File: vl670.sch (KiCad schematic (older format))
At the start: 56 parts, among them J1 Conn_01x07_Male, J2 USB_C_Receptacle, J3 Conn_01x07_Male, J4 USB3_A Receptacle, J5 Conn_01x02_Male, U2 VL670, U4 TPS2061C-PXLI, Y1 25MHz

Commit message: First private release.
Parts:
- removed C15: 1uF, Capacitor_SMD:C_0603_1608Metric_Pad1.08x0.95mm_HandSolder, symbol Device:C
- removed C23, C24: 330nF, Capacitor_SMD:C_0603_1608Metric, symbol Device:C_Small
- removed JP3: SolderJumper_2_Bridged, Jumper:SolderJumper-2_P1.3mm_Bridged_RoundedPad1.0x1.5mm, symbol Jumper:SolderJumper_2_Bridged
- added C7, C8: 220nF, Capacitor_SMD:C_0603_1608Metric_Pad1.08x0.95mm_HandSolder, symbol Device:C_Small
- added R15: 10k, Resistor_SMD:R_0603_1608Metric_Pad0.98x0.95mm_HandSolder, symbol Device:R_US
- added R19: 0R, Resistor_SMD:R_0603_1608Metric_Pad0.98x0.95mm_HandSolder, symbol Device:R_US
- C10, C11: Grade (none) -> NP0
- C31: renamed from C1; value 1uF -> 470nF
- C32: renamed from C2; value 1uF -> 470nF
- C33: renamed from C3; value 1uF -> 470nF
- C34: renamed from C4; value 1uF -> 470nF
- C35: renamed from C5; value 1uF -> 470nF
- D10, D11, D12, D13, D15, D16, D17, D18, D8, D9: value D_TVS -> ESD7951S; footprint Diode_SMD:D_SOD-923 -> Diode_SMD:D_SOD-523
- D14, D7: footprint Diode_SMD:D_SOD-923 -> Diode_SMD:D_SOD-523
- J2: footprint Connector_USB:USB_C_Receptacle_Amphenol_12401548E4-2A -> vl670:USB_C_Receptacle_XKB_U262-241N-4BV60
- J4: footprint Connector_USB:USB3_A_Molex_48393-001 -> vl670:USB3_A_Receptacle_Wuerth_692112030100_Horizontal
- L1: footprint Inductor_SMD:L_0603_1608Metric_Pad1.05x0.95mm_HandSolder -> Inductor_SMD:L_1008_2520Metric_Pad1.43x2.20mm_HandSolder; Brand (none) -> L1: Sunlord; Part Number (none) -> SPH252012H4R7MT
- renumbered C6 to C41, C7 to C42, C8 to C43, C9 to C44, C17 to C51, C18 to C52, C14 to C61, C16 to C62
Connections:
- net labels added: DN_SSRX+, DN_SSRX-, DN_SSTX+, DN_SSTX-, DN_TX_AC+, DN_TX_AC-, D_DEMUX+, D_DEMUX-, SSRX_DEMUX+, SSRX_DEMUX-, SSTX_DEMUX+, SSTX_DEMUX-, ~EXT_RESET
- net labels removed: D+, D-, DN_USB3RX+, DN_USB3RX-, DN_USB3TX+, DN_USB3TX-, TX+, TX-
- wire segments 313 -> 319
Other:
- note added: "By default, both VL670 and ISP header\nare connected, to allow probing SPI\nwhile VL670 is running.\n\nTo program the EEPROM, a programmer\nmust pull ~ISP_ENABLE~ low from the ISP\nheader (bridge pin 6 & 7 on J1), to\navoid bus contention."
- note added: "C44 MUST be close to L1"
- note added: "PCB\nlayout-specific\n components"
- note added: "close to VL670, one per pin"
- note removed: "By default, both VL670 and ISP header\nare connected, to allow probing SPI\nwhile VL670 is running.\n\nTo program the EEPROM, a programmer\nmust pull ~ISP_ENABLE~ low from the ISP\nheader, to avoid bus contention."
- moved on the sheet: C13, C31, C32, C33, C34, C35, C41, C42, C43, C44, C51, C52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

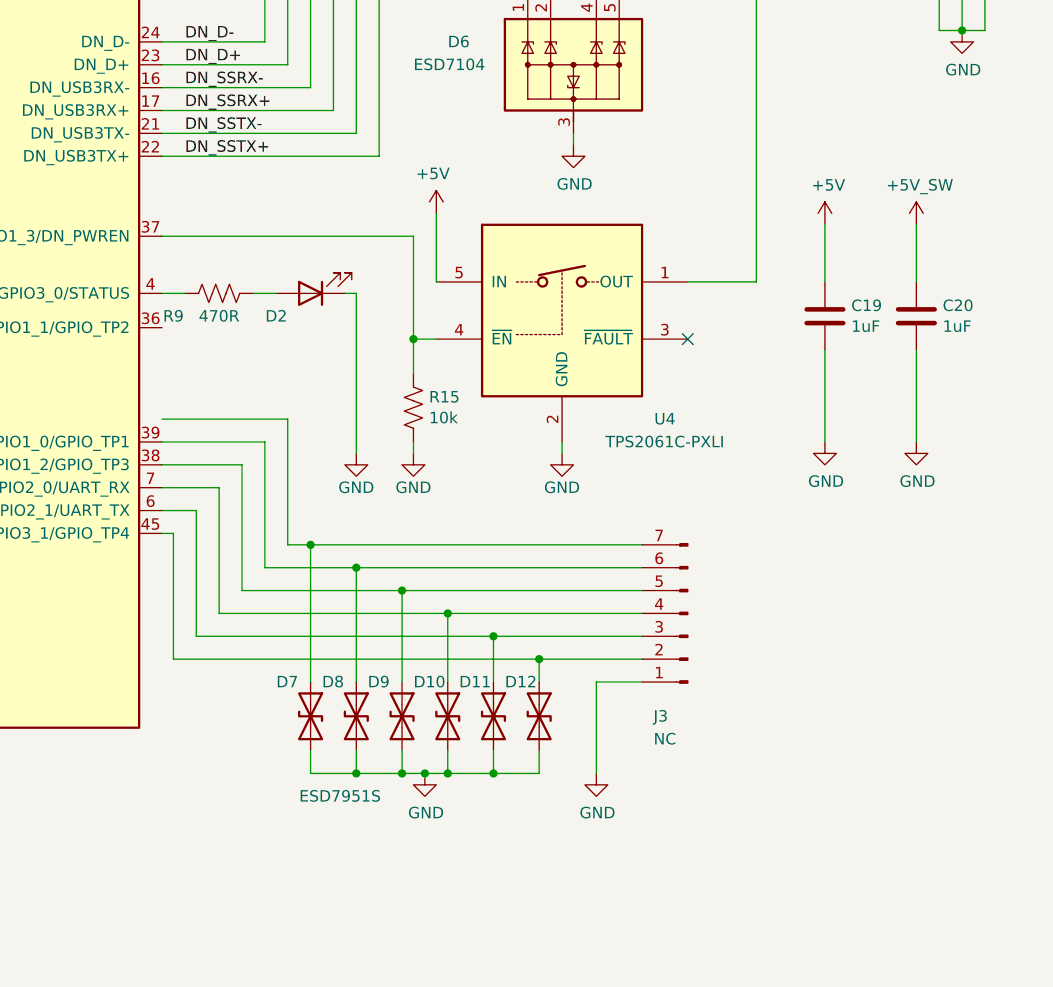
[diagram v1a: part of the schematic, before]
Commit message: Change GPIO connections to match firmware.
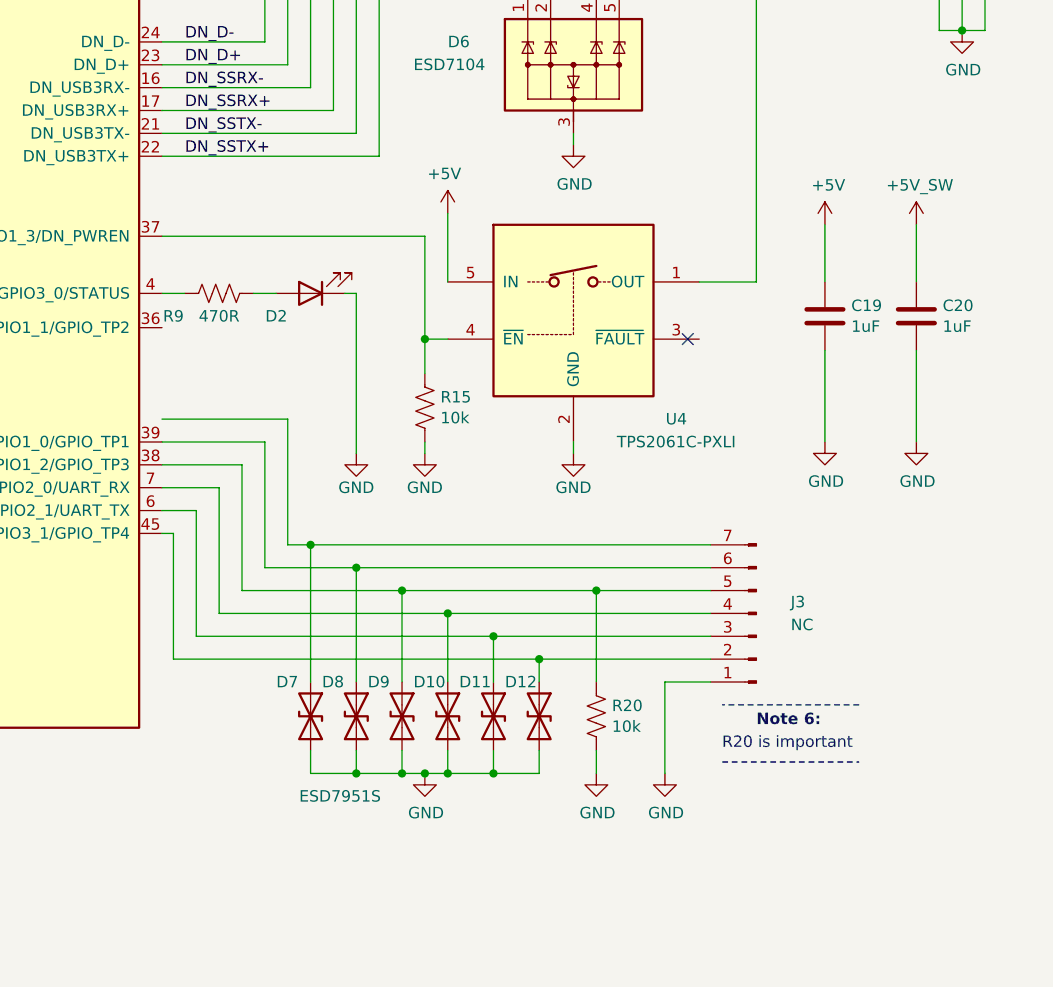
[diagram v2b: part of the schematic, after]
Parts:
- added R20: 10k, Resistor_SMD:R_0603_1608Metric_Pad0.98x0.95mm_HandSolder, symbol Device:R_US
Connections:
- net GND: now also R20.2
- net at D9.1 (A1), J3.5 (Pin_5), U2.38 (GPIO1_2/GPIO_TP3): now also R20.1
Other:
- note added: "Note 6:"
- note added: "R20 is important"
- moved on the sheet: J3, R15, U4
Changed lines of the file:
@@
 L power:GND #PWR0115
 U 1 1 60701D89
-P 9050 4900
-F 0 "#PWR0115" H 9050 4650 50  0001 C CNN
-F 1 "GND" H 9050 4750 50  0000 C CNN
-F 2 "" H 9050 4900 50  0001 C CNN
-F 3 "" H 9050 4900 50  0001 C CNN
-	1    9050 4900
+P 9100 4900
+F 0 "#PWR0115" H 9100 4650 50  0001 C CNN
+F 1 "GND" H 9100 4750 50  0000 C CNN
+F 2 "" H 9100 4900 50  0001 C CNN
+F 3 "" H 9100 4900 50  0001 C CNN
+	1    9100 4900
 	-1   0    0    -1
 $EndComp
@@
 L Connector:Conn_01x07_Male J3
 U 1 1 61CF71E3
-P 9600 5600
-F 0 "J3" H 9750 6050 50  0000 R CNN
-F 1 "Conn_01x07_Male" H 9572 5623 50  0001 R CNN
-F 2 "Connector_PinHeader_2.54mm:PinHeader_1x07_P2.54mm_Vertical" H 9600 5600 50  0001 C CNN
-F 3 "~" H 9600 5600 50  0001 C CNN
-F 4 "NC" H 9700 6150 50  0000 C CNN "Install"
-	1    9600 5600
+P 9900 5600
+F 0 "J3" H 9750 5550 50  0000 R CNN
+F 1 "Conn_01x07_Male" H 9872 5623 50  0001 R CNN
+F 2 "Connector_PinHeader_2.54mm:PinHeader_1x07_P2.54mm_Vertical" H 9900 5600 50  0001 C CNN
+F 3 "~" H 9900 5600 50  0001 C CNN
+F 4 "NC" H 9700 5650 50  0000 C CNN "Install"
+	1    9900 5600
 	-1   0    0    1
 $EndComp
@@
 L vl670:TPS2061C U4
 U 1 1 605C86BA
-P 9050 4200
-F 0 "U4" H 9500 3650 50  0000 C CNN
-F 1 "TPS2061C-PXLI" H 9500 3550 50  0000 C CNN
-F 2 "Package_TO_SOT_SMD:SOT-23-5_HandSoldering" H 9050 4700 50  0001 C CNN
-F 3 "https://www.ti.com/lit/gpn/tps2061c" H 9000 4500 50  0001 C CNN
-	1    9050 4200
+P 9100 4200
+F 0 "U4" H 9550 3650 50  0000 C CNN
+F 1 "TPS2061C-PXLI" H 9550 3550 50  0000 C CNN
+F 2 "Package_TO_SOT_SMD:SOT-23-5_HandSoldering" H 9100 4700 50  0001 C CNN
+F 3 "https://www.ti.com/lit/gpn/tps2061c" H 9050 4500 50  0001 C CNN
+	1    9100 4200
 	1    0    0    -1
 $EndComp
@@
 L power:GND #PWR0126
 U 1 1 60071875
-P 9200 6300
-F 0 "#PWR0126" H 9200 6050 50  0001 C CNN
-F 1 "GND" H 9205 6127 50  0000 C CNN
-F 2 "" H 9200 6300 50  0001 C CNN
-F 3 "" H 9200 6300 50  0001 C CNN
-	1    9200 6300
-	1    0    0    -1
-$EndComp
-Wire Wire Line
-	9200 5900 9400 5900
-Wire Wire Line
-	8400 3950 8400 4400
-Wire Wire Line
-	7300 3950 8400 3950
-Wire Wire Line
-	8400 4400 8500 4400
+P 9500 6300
+F 0 "#PWR0126" H 9500 6050 50  0001 C CNN
+F 1 "GND" H 9505 6127 50  0000 C CNN
+F 2 "" H 9500 6300 50  0001 C CNN
+F 3 "" H 9500 6300 50  0001 C CNN
+	1    9500 6300
+	1    0    0    -1
+$EndComp
+Wire Wire Line
+	9500 5900 9700 5900
 Wire Wire Line
 	7300 4200 7400 4200
@@
 L power:+5V #PWR0112
 U 1 1 605CDF9A
-P 8500 3850
-F 0 "#PWR0112" H 8500 3700 50  0001 C CNN
-F 1 "+5V" H 8515 4023 50  0000 C CNN
-F 2 "" H 8500 3850 50  0001 C CNN
-F 3 "" H 8500 3850 50  0001 C CNN
-	1    8500 3850
+P 8550 3850
+F 0 "#PWR0112" H 8550 3700 50  0001 C CNN
+F 1 "+5V" H 8565 4023 50  0000 C CNN
+F 2 "" H 8550 3850 50  0001 C CNN
+F 3 "" H 8550 3850 50  0001 C CNN
+	1    8550 3850
 	-1   0    0    -1
 $EndComp
@@
 	1    0    0    -1
 $EndComp
-Wire Wire Line
-	9600 4150 9900 4150
 Connection ~ 9900 1800
 Wire Wire Line
@@
 Connection ~ 8950 5800
 Wire Wire Line
-	8950 5800 9400 5800
-Wire Wire Line
-	8750 5700 9400 5700
-Wire Wire Line
-	8550 5600 9400 5600
-Wire Wire Line
-	8350 5500 9400 5500
-Wire Wire Line
-	8150 5400 9400 5400
-Wire Wire Line
-	7950 5300 9400 5300
-Wire Wire Line
-	9200 5900 9200 6300
+	9500 5900 9500 6300
 Wire Wire Line
 	7950 6300 8150 6300
@@
 	6600 1800 6700 1800
 Wire Wire Line
-	8500 3850 8500 4150
-Wire Wire Line
-	9050 4850 9050 4900
+	8550 3850 8550 4150
+Wire Wire Line
+	9100 4850 9100 4900
 Wire Wire Line
 	8150 4200 8150 4900
@@
 	1    0    0    -1
 $EndComp
-Connection ~ 8400 4400
 $Comp
 L Device:R_US R15
 U 1 1 608A3AA8
-P 8400 4700
-F 0 "R15" H 8468 4746 50  0000 L CNN
-F 1 "10k" H 8468 4655 50  0000 L CNN
-F 2 "Resistor_SMD:R_0603_1608Metric_Pad0.98x0.95mm_HandSolder" V 8440 4690 50  0001 C CNN
-F 3 "~" H 8400 4700 50  0001 C CNN
-	1    8400 4700
-	1    0    0    -1
-$EndComp
-Wire Wire Line
-	8400 4550 8400 4400
+P 8450 4700
+F 0 "R15" H 8518 4746 50  0000 L CNN
+F 1 "10k" H 8518 4655 50  0000 L CNN
+F 2 "Resistor_SMD:R_0603_1608Metric_Pad0.98x0.95mm_HandSolder" V 8490 4690 50  0001 C CNN
+F 3 "~" H 8450 4700 50  0001 C CNN
+	1    8450 4700
+	1    0    0    -1
+$EndComp
 $Comp
 L power:GND #PWR0111
 U 1 1 608DDF82
-P 8400 4900
-F 0 "#PWR0111" H 8400 4650 50  0001 C CNN
-F 1 "GND" H 8400 4750 50  0000 C CNN
-F 2 "" H 8400 4900 50  0001 C CNN
-F 3 "" H 8400 4900 50  0001 C CNN
-	1    8400 4900
+P 8450 4900
+F 0 "#PWR0111" H 8450 4650 50  0001 C CNN
+F 1 "GND" H 8450 4750 50  0000 C CNN
+F 2 "" H 8450 4900 50  0001 C CNN
+F 3 "" H 8450 4900 50  0001 C CNN
+	1    8450 4900
 	-1   0    0    -1
 $EndComp
 Wire Wire Line
-	8400 4850 8400 4900
+	8450 4850 8450 4900
 Wire Wire Line
 	8150 4200 8100 4200
@@
 Wire Wire Line
 	8900 2550 8800 2750
+$Comp
+L Device:R_US R20
+U 1 1 61D6C1E1
+P 9200 6050
+F 0 "R20" H 9268 6096 50  0000 L CNN
+F 1 "10k" H 9268 6005 50  0000 L CNN
+F 2 "Resistor_SMD:R_0603_1608Metric_Pad0.98x0.95mm_HandSolder" V 9240 6040 50  0001 C CNN
+F 3 "~" H 9200 6050 50  0001 C CNN
+	1    9200 6050
+	1    0    0    -1
+$EndComp
+Wire Wire Line
+	9200 6200 9200 6300
+$Comp
+L power:GND #PWR0183
+U 1 1 61E4C0B1
+P 9200 6300
+F 0 "#PWR0183" H 9200 6050 50  0001 C CNN
+F 1 "GND" H 9205 6127 50  0000 C CNN
+F 2 "" H 9200 6300 50  0001 C CNN
+F 3 "" H 9200 6300 50  0001 C CNN
+	1    9200 6300
+	1    0    0    -1
+$EndComp
+Wire Wire Line
+	8950 5800 9700 5800
+Wire Wire Line
+	8750 5700 9700 5700
+Wire Wire Line
+	8550 5600 9700 5600
+Wire Wire Line
+	7950 5300 9700 5300
+Wire Notes Line
+	9750 6250 10350 6250
+Wire Notes Line
+	10350 6000 9750 6000
+Wire Wire Line
+	8150 5400 9700 5400
+Wire Wire Line
+	9200 5500 9700 5500
+Wire Wire Line
+	8350 5500 9200 5500
+Connection ~ 9200 5500
+Wire Wire Line
+	9200 5900 9200 5500
+Wire Wire Line
+	8450 3950 8450 4400
+Wire Wire Line
+	7300 3950 8450 3950
+Wire Wire Line
+	8550 4400 8450 4400
+Connection ~ 8450 4400
+Wire Wire Line
+	8450 4400 8450 4550
+Wire Wire Line
+	9650 4150 9900 4150
+Text Notes 9750 6200 0    50   ~ 0
+R20 is important
+Text Notes 9900 6100 0    50   ~ 10
+Note 6:
 $EndSCHEMATC

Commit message: various changes for v0.01 public release.
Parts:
- added R21: 10k, Resistor_SMD:R_0603_1608Metric_Pad0.98x0.95mm_HandSolder, symbol Device:R_US
- C7, C8: value 220nF -> 100nF
- D14, D7: value ESD7951S -> ESD5B5.0ST1G-N
- J3: Install NC -> (none)
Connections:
- net GND: now also R21.2
- net at D8.1 (A1), J3.6 (Pin_6), U2.39 (GPIO1_0/GPIO_TP1): now also R21.1
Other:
- note added: "By default, both VL670 and ISP header\nare connected, to allow probing SPI\nwhile VL670 is running.\n\nTo program the EEPROM, a programmer\nmust pull ~ISP_ENABLE~ low from the ISP\nheader (bridge pin 6 "~EN~"& 7 "GND" on\nJ1), to avoid bus contention."
- note added: "Cut JP2 to isolate USB\nconnector from global 5 V\nrail for debugging with\nexternal power."
- note added: "Internal 3.3 V, 1.5 V, 1.2 V supplies\nshould only power VL670 & EEPROM\nand the SPI multiplexers.\nDON'T CONNECT TO OTHER CHIPS."
- note removed: "By default, both VL670 and ISP header\nare connected, to allow probing SPI\nwhile VL670 is running.\n\nTo program the EEPROM, a programmer\nmust pull ~ISP_ENABLE~ low from the ISP\nheader (bridge pin 6 & 7 on J1), to\navoid bus contention."
- note removed: "Cut jumpers to isolate USB\nconnector from global 5 V\nrail for debugging with\nexternal power."
- note removed: "Internal 3.3 V/1.5 V LDO & 1.2 V\nDCDC should only power VL670 & \nEEPROM. DON'T CONNECT TO OTHER\nCHIPS."
- moved on the sheet: J3

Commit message: rename components and footprints.
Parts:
- J4: footprint vl670:USB3_A_Receptacle_Wuerth_692112030100_Horizontal -> vl670:USB3_A_Receptacle_XKB_U231-091N-4BLRA00-S-1
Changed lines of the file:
@@
 F 0 "J4" H 10700 2950 50  0000 C CNN
 F 1 "USB3_A Receptacle" H 10700 2850 50  0000 C CNN
-F 2 "vl670:USB3_A_Receptacle_Wuerth_692112030100_Horizontal" H 10850 2300 50  0001 C CNN
+F 2 "vl670:USB3_A_Receptacle_XKB_U231-091N-4BLRA00-S-1" H 10850 2300 50  0001 C CNN
 F 3 "~" H 10850 2300 50  0001 C CNN
 	1    10700 2200

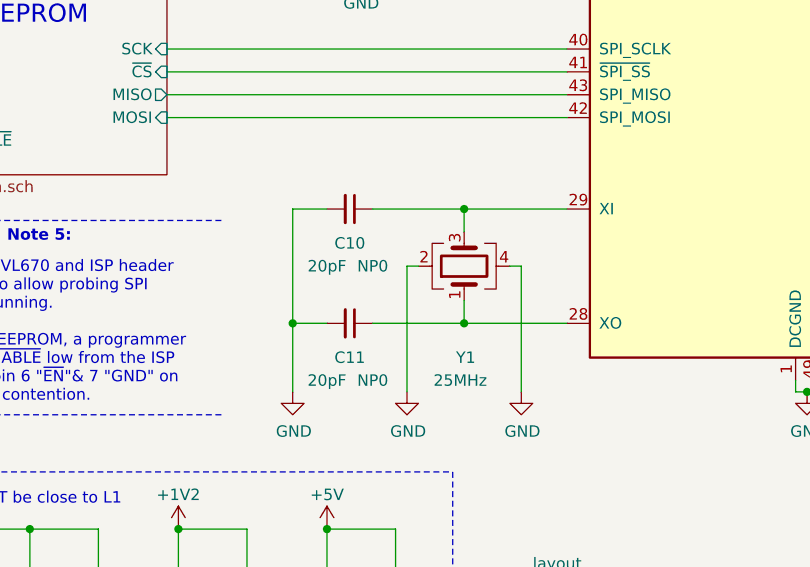
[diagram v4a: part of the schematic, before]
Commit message: vl670.sch: change crystal and loading capacitance
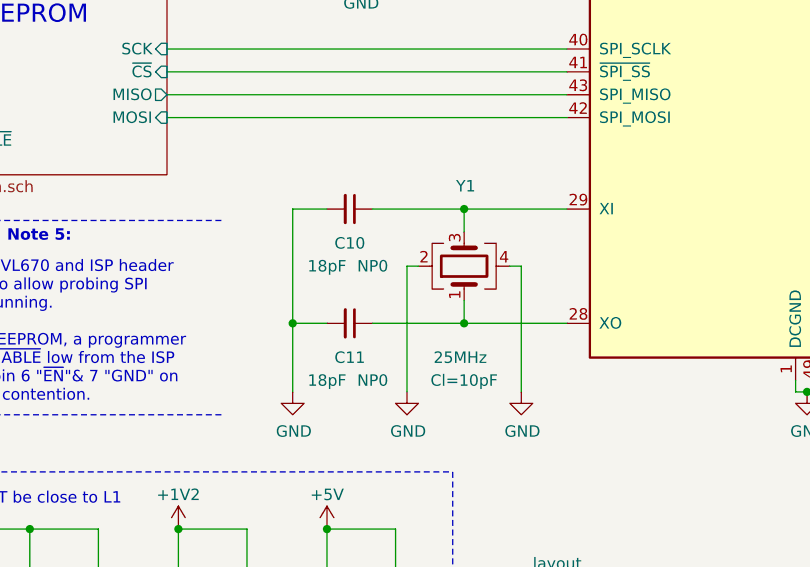
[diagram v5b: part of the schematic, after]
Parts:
- C10, C11: value 20pF -> 18pF
- Y1: Parameter (none) -> Cl=10pF
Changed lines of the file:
@@
 	4800 5850 4800 5950
-$Comp
-L power:GND #PWR0102
-U 1 1 5F845F1C
-P 4050 6250
-AR Path="/5F845F1C" Ref="#PWR0102"  Part="1"
-AR Path="/5E73BE76/5F845F1C" Ref="#PWR039"  Part="1"
-AR Path="/5EDD0BB0/5F845F1C" Ref="#PWR?"  Part="1"
-F 0 "#PWR0102" H 4050 6000 50  0001 C CNN
-F 1 "GND" H 4055 6077 50  0000 C CNN
-F 2 "" H 4050 6250 50  0001 C CNN
-F 3 "" H 4050 6250 50  0001 C CNN
-	1    4050 6250
-	1    0    0    -1
-$EndComp
 $Comp
 L Device:Crystal_GND24 Y1
 U 1 1 5F845F29
 P 4800 5700
-F 0 "Y1" V 4400 5650 50  0000 L CNN
-F 1 "25MHz" V 4300 5600 50  0000 L CNN
+F 0 "Y1" V 5150 5650 50  0000 L CNN
+F 1 "25MHz" V 4400 5600 50  0000 L CNN
 F 2 "Crystal:Crystal_SMD_3225-4Pin_3.2x2.5mm" H 4800 5700 50  0001 C CNN
 F 3 "~" H 4800 5700 50  0001 C CNN
+F 4 "Cl=10pF" V 4300 5700 50  0000 C CNN "Parameter"
 	1    4800 5700
 	0    -1   -1   0
@@
 AR Path="/5EDD0BB0/5F845F1B" Ref="C?"  Part="1"
 F 0 "C11" V 4450 5950 50  0000 C CNN
-F 1 "20pF" V 4550 5850 50  0000 C CNN
+F 1 "18pF" V 4550 5850 50  0000 C CNN
 F 2 "Capacitor_SMD:C_0603_1608Metric_Pad1.08x0.95mm_HandSolder" H 4300 5950 50  0001 C CNN
 F 3 "~" H 4300 5950 50  0001 C CNN
@@
 AR Path="/5EDD0BB0/5E741279" Ref="C?"  Part="1"
 F 0 "C10" V 4450 5450 50  0000 C CNN
-F 1 "20pF" V 4550 5350 50  0000 C CNN
+F 1 "18pF" V 4550 5350 50  0000 C CNN
 F 2 "Capacitor_SMD:C_0603_1608Metric_Pad1.08x0.95mm_HandSolder" H 4300 5450 50  0001 C CNN
 F 3 "~" H 4300 5450 50  0001 C CNN
@@
 Wire Notes Line
 	3650 4300 4250 4300
+$Comp
+L power:GND #PWR0102
+U 1 1 5F845F1C
+P 4050 6250
+AR Path="/5F845F1C" Ref="#PWR0102"  Part="1"
+AR Path="/5E73BE76/5F845F1C" Ref="#PWR039"  Part="1"
+AR Path="/5EDD0BB0/5F845F1C" Ref="#PWR?"  Part="1"
+F 0 "#PWR0102" H 4050 6000 50  0001 C CNN
+F 1 "GND" H 4055 6077 50  0000 C CNN
+F 2 "" H 4050 6250 50  0001 C CNN
+F 3 "" H 4050 6250 50  0001 C CNN
+	1    4050 6250
+	1    0    0    -1
+$EndComp
 $EndSCHEMATC

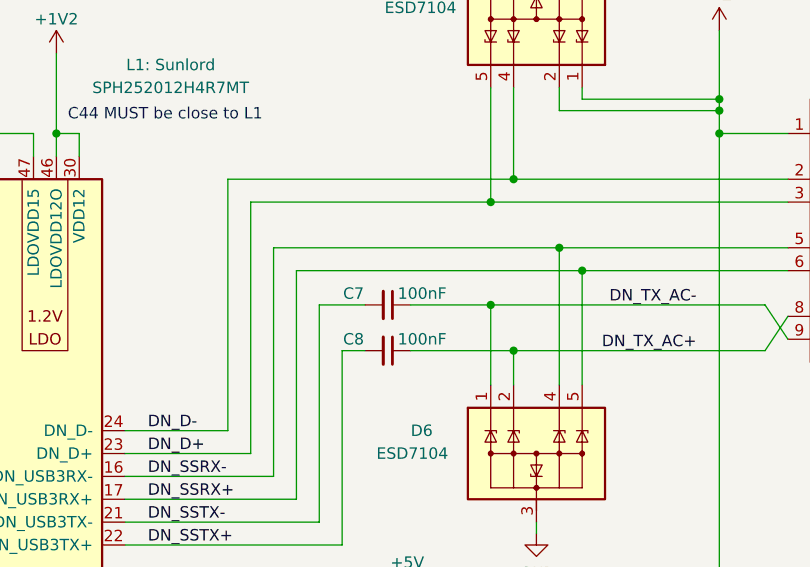
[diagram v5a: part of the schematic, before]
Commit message: vl670.sch: change downstream capacitance value to 220 uF.
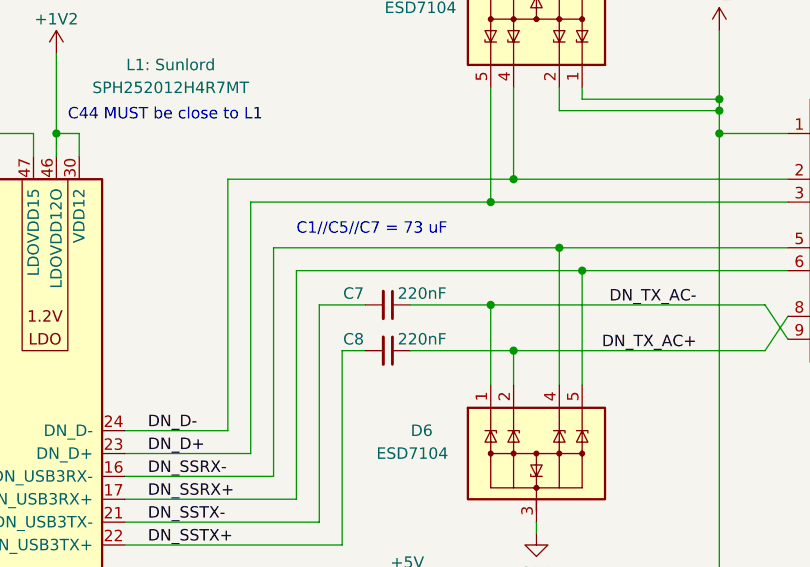
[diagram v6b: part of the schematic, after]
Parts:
- C7, C8: value 100nF -> 220nF
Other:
- note added: "C1//C5//C7 = 73 uF"
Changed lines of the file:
@@
 Title "Main Schematic - VL670 Development Board"
 Date "2021-06-29"
-Rev "v0.01"
+Rev "v0.01-dev"
 Comp "Copyright (C) 2021 Tom Li (niconiconi)"
 Comment1 "https://creativecommons.org/publicdomain/zero/1.0/"
@@
 P 8450 2750
 F 0 "C8" V 8400 2600 50  0000 C CNN
-F 1 "100nF" V 8400 2900 50  0000 C CNN
+F 1 "220nF" V 8400 2900 50  0000 C CNN
 F 2 "Capacitor_SMD:C_0603_1608Metric_Pad1.08x0.95mm_HandSolder" H 8450 2750 50  0001 C CNN
 F 3 "~" H 8450 2750 50  0001 C CNN
@@
 P 8450 2550
 F 0 "C7" V 8400 2400 50  0000 C CNN
-F 1 "100nF" V 8400 2700 50  0000 C CNN
+F 1 "220nF" V 8400 2700 50  0000 C CNN
 F 2 "Capacitor_SMD:C_0603_1608Metric_Pad1.08x0.95mm_HandSolder" H 8450 2550 50  0001 C CNN
 F 3 "~" H 8450 2550 50  0001 C CNN
@@
 	1    0    0    -1
 $EndComp
+Text Notes 8050 2250 0    50   ~ 0
+C1//C5//C7 = 73 uF
 $EndSCHEMATC
